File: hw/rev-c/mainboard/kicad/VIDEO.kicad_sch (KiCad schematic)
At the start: 1 part, among them J7 VIDEO

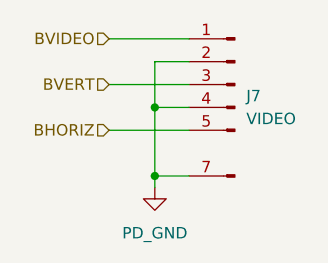
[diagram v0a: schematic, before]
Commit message: hw: PD_GND -> GND
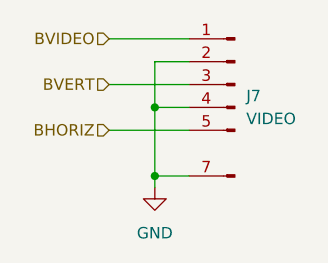
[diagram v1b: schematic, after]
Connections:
- net PD_GND renamed GND
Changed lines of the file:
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@@
 	)
 	(symbol
-		(lib_id "PET:PD_GND")
+		(lib_id "power:GND")
 		(at 137.16 101.6 0)
 		(unit 1)
@@
 			)
 		)
-		(property "Value" "PD_GND"
+		(property "Value" "GND"
 			(at 137.16 106.68 0)
 			(effects
@@
 			)
 		)
-		(property "Description" ""
+		(property "Description" "Power symbol creates a global label with name \"GND\" , ground"
 			(at 137.16 101.6 0)
 			(effects

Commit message: hw: fix wire/grid violations in schematic
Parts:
- J7: symbol Retrocomputing:CBM_PET_VIDEO_Conn_Keyed -> EconoPET:CBM_PET_VIDEO_Conn_Keyed
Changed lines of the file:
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@@
 	)
 	(symbol
-		(lib_id "Retrocomputing:CBM_PET_VIDEO_Conn_Keyed")
+		(lib_id "EconoPET:CBM_PET_VIDEO_Conn_Keyed")
 		(at 146.05 92.71 0)
 		(mirror y)

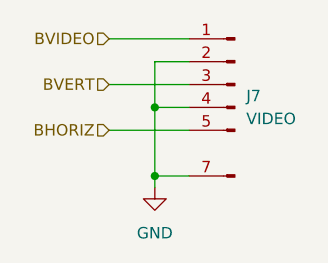
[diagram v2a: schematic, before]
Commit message: hw: renumber reference designators
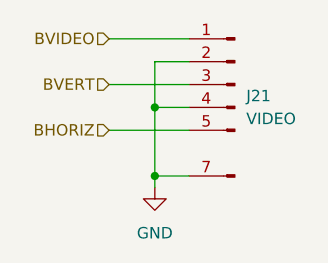
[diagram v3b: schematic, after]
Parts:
- renumbered J7 to J21
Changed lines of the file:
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@@
 		(dnp no)
 		(fields_autoplaced yes)
-		(property "Reference" "#PWR0143"
+		(property "Reference" "#PWR0145"
 			(at 137.16 107.95 0)
 			(effects
@@
 			(project ""
 				(path "/2eea20e6-112c-411a-b615-885ae773135a/1dc0595f-3832-49f8-98ab-9c5f13feffce"
-					(reference "#PWR0143")
+					(reference "#PWR0145")
 					(unit 1)
 				)
@@
 		(dnp no)
 		(fields_autoplaced yes)
-		(property "Reference" "J7"
+		(property "Reference" "J21"
 			(at 147.32 91.4399 0)
 			(effects
@@
 			(project ""
 				(path "/2eea20e6-112c-411a-b615-885ae773135a/1dc0595f-3832-49f8-98ab-9c5f13feffce"
-					(reference "J7")
+					(reference "J21")
 					(unit 1)
 				)

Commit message: hw: match original PET designators for connectors
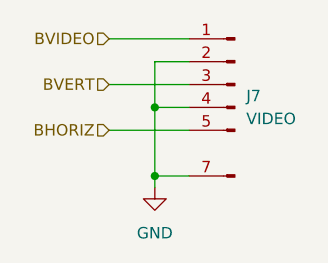
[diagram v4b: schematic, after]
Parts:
- renumbered J21 to J7
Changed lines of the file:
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@@
 		(dnp no)
 		(fields_autoplaced yes)
-		(property "Reference" "J21"
+		(property "Reference" "J7"
 			(at 147.32 91.4399 0)
 			(effects
@@
 			(project ""
 				(path "/2eea20e6-112c-411a-b615-885ae773135a/1dc0595f-3832-49f8-98ab-9c5f13feffce"
-					(reference "J21")
+					(reference "J7")
 					(unit 1)
 				)

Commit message: hw: tidy warnings
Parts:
- J7: footprint PET:PET_Video -> EconoPET:PET_Video
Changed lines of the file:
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@@
 			)
 		)
-		(property "Footprint" "PET:PET_Video"
+		(property "Footprint" "EconoPET:PET_Video"
 			(at 146.05 92.71 0)
 			(effects
